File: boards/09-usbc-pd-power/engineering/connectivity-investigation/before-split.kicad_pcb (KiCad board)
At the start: 4 copper layers, 100 x 65 mm, 47 parts, among them J1 USB-C PD INPUT, J2 5V OUTPUT, J3 I2C HOST 3V3, Q1 AO4407A, Q2 AO4407A, U1 STUSB4500QTR, U2 TPS54302DDCR, U3 INA226AIDGSR, U4 TLV76033DBZR

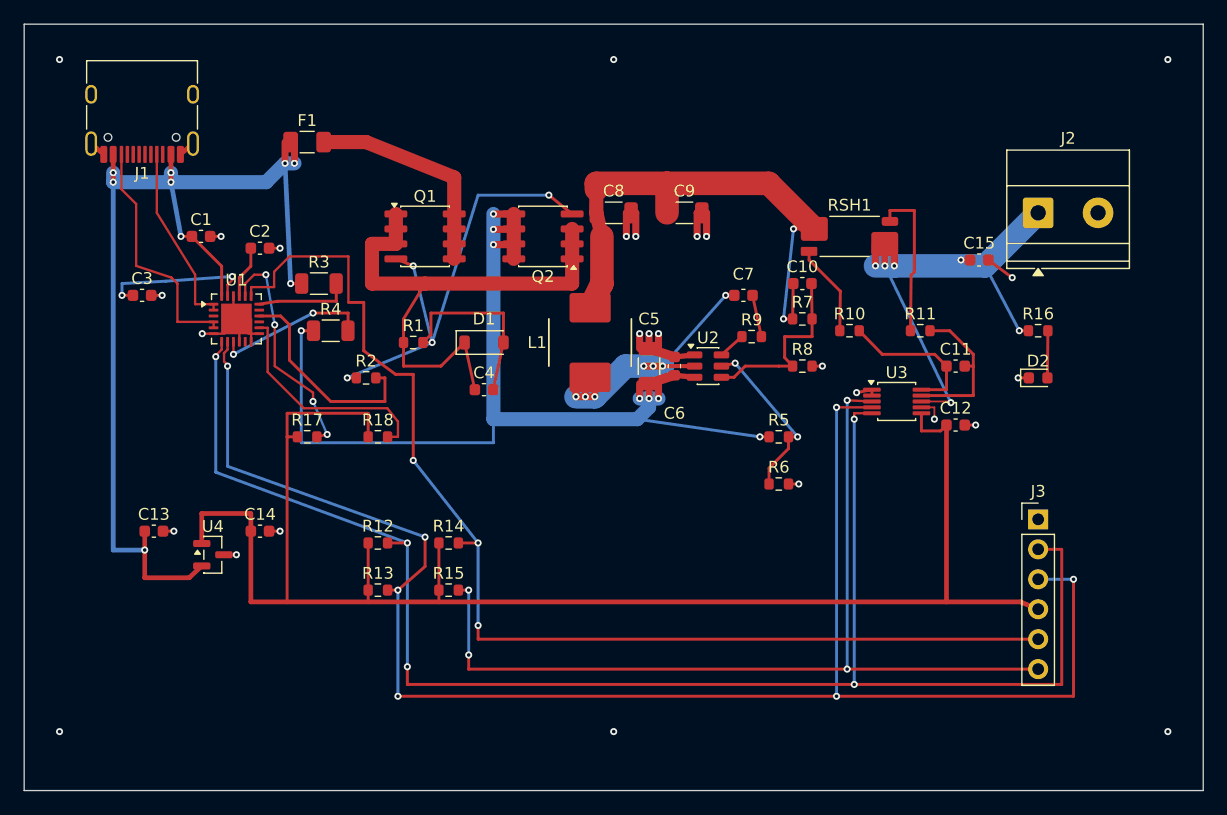
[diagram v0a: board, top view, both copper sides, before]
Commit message: feat(boards): complete board09 routing and inner ground planes
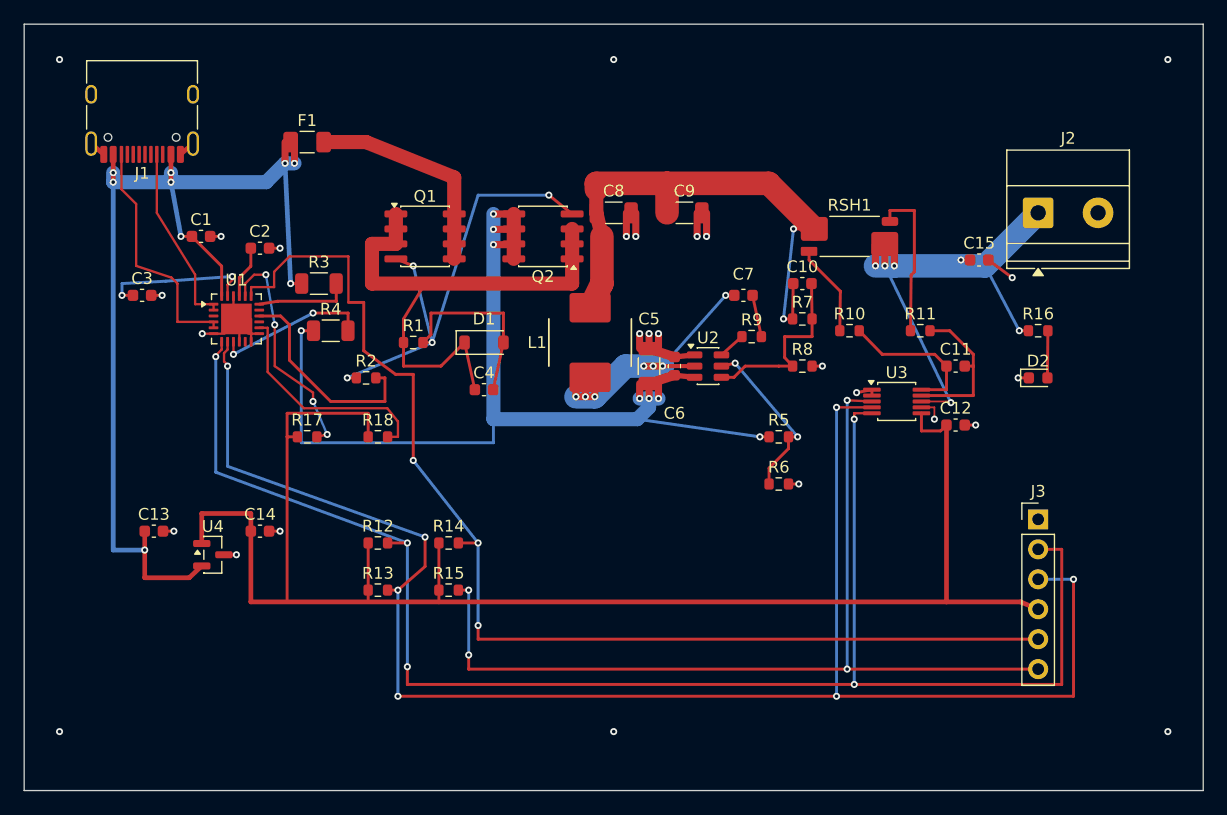
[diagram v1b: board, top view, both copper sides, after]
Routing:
- net GND: track 44.6 -> 43.0 mm
